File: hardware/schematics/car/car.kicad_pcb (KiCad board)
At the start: 2 copper layers, 30.2 x 17.9 mm, 18 parts, among them M1 Motor_Servo, Q1 Q_PMOS_Depletion, SW1 RotaryEncoder, SW2 SW_Push, SW3 SW_Push, U1 VL53L0CXV0DH1, U10 Mini-560, U2 VL53L0CXV0DH1, U3 VL53L0CXV0DH1, U4 Pixy2, U5 TXS0108EPW, U6 TB6612FNG, U7 SparkFun OTOS, U9 Mini-360

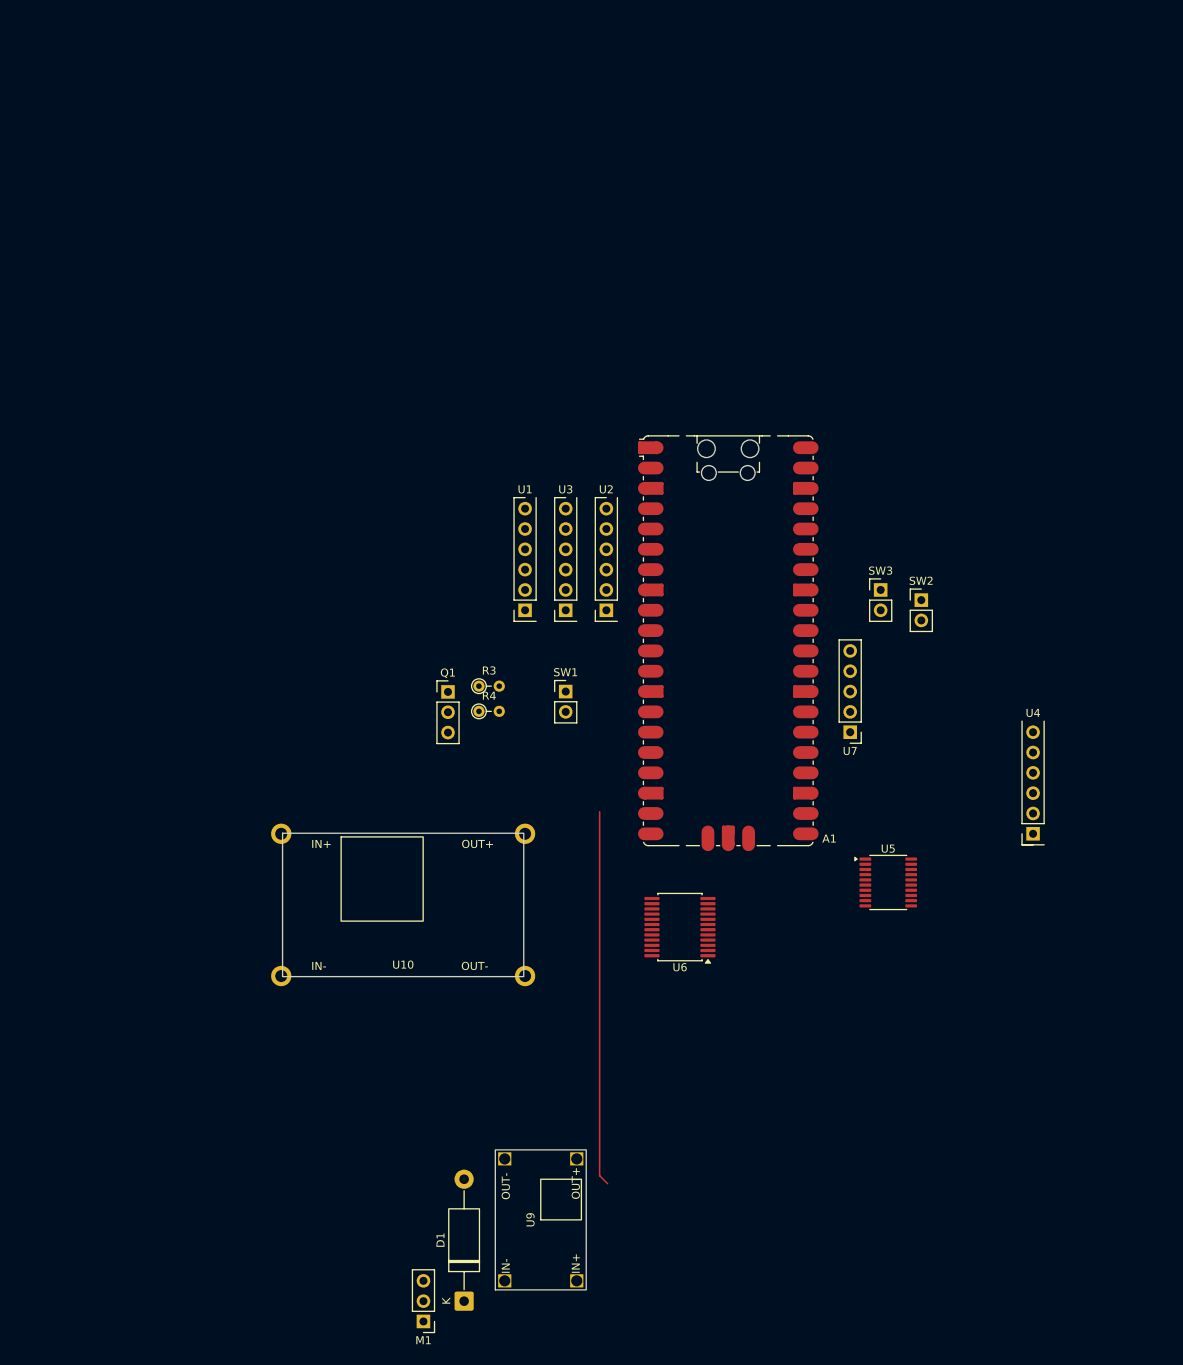
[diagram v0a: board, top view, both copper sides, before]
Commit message: [Schematic] update pcb components
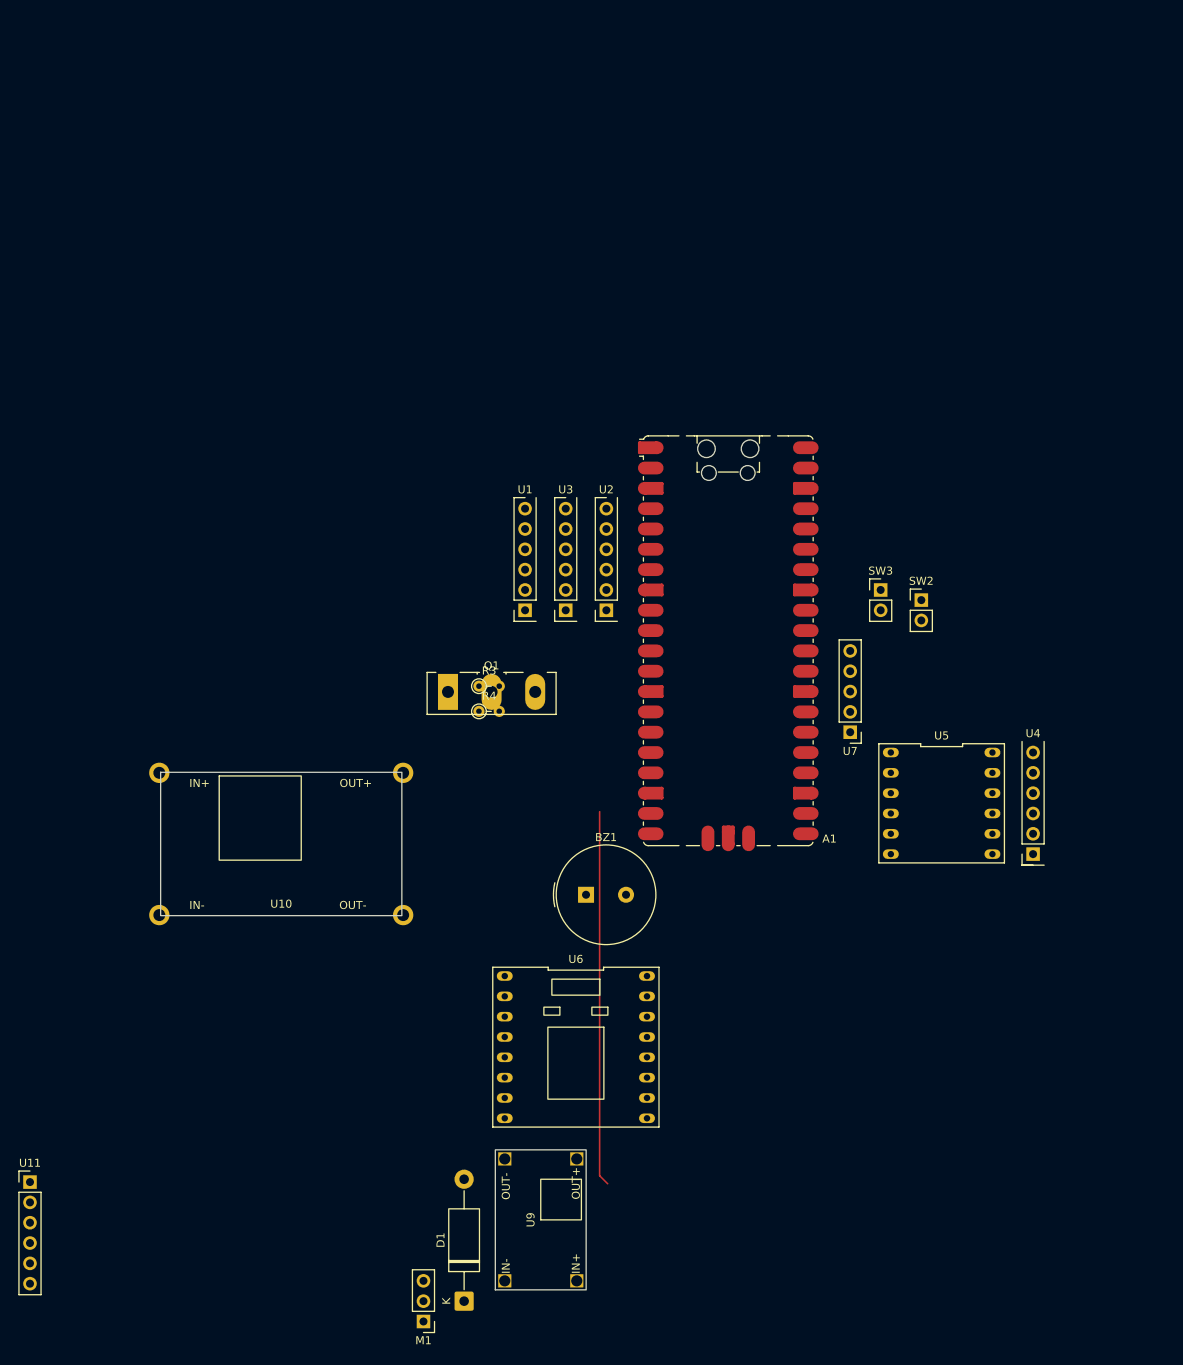
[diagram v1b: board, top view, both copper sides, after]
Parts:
- removed SW1: RotaryEncoder, Connector_PinHeader_2.54mm:PinHeader_1x02_P2.54mm_Vertical
- added BZ1: Buzzer, Buzzer_Beeper:Buzzer_TDK_PS1240P02BT_D12.2mm_H6.5mm, F.Cu at (114.3, 119.4)
- added U11: JGA25-37x, Connector_PinHeader_2.54mm:PinHeader_1x06_P2.54mm_Vertical, F.Cu at (44.8, 155.3)
- Q1: value Q_PMOS_Depletion -> PMOS; footprint Connector_PinHeader_2.54mm:PinHeader_1x03_P2.54mm_Vertical -> Package_TO_SOT_THT:TO-247-3_Vertical
- U5: value TXS0108EPW -> Level shifter; footprint Package_SO:TSSOP-20_4.4x6.5mm_P0.65mm -> xlnc-foot:LevelShifter_4channel_bidirectional
- U6: footprint Package_SO:SSOP-24_5.3x8.2mm_P0.65mm -> xlnc-foot:TB6612FNG_Breakout_Sparkfun
- moved U6 19.9 mm to (113.0, 138.4), turned to -90 degrees
- moved U10 17.0 mm to (76.2, 113.0)
- moved U5 11.9 mm to (158.8, 108.0), turned to -90 degrees
- moved U4 2.54 mm to (170.2, 101.6)
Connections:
- Q1 pad 1: (no net) -> +5V
- Q1 pad 2: (no net) -> Net-(A1-VBUS)
- Q1 pad 3: (no net) -> Net-(A1-VSYS)
- U5 pad 1: Net-(A1-GPIO16) -> Net-(A1-GPIO19)
- U5 pad 10: +3.3V -> +5V
- U5 pad 11: GND -> Net-(U4-SPI_SCK)
- U5 pad 12: unconnected-(U5-B8-Pad12) -> Net-(U4-MOSI/TX)
- U5 pad 2: +3.3V -> Net-(A1-GPIO18)
- U5 pad 3: Net-(A1-GPIO17) -> +3.3V
- U5 pad 4: Net-(A1-GPIO18) -> GND
- U5 pad 5: Net-(A1-GPIO19) -> Net-(A1-GPIO17)
- U5 pad 6: unconnected-(U5-A5-Pad6) -> Net-(A1-GPIO16)
- U5 pad 7: unconnected-(U5-A6-Pad7) -> Net-(U4-MISO/RX)
- U5 pad 8: unconnected-(U5-A7-Pad8) -> Net-(U4-SPI_SS)
- U5 pad 9: unconnected-(U5-A8-Pad9) -> GND
- U6 pad 1: Net-(M2-+) -> Net-(U11-M1)
- U6 pad 5: Net-(M2--) -> Net-(U11-M2)

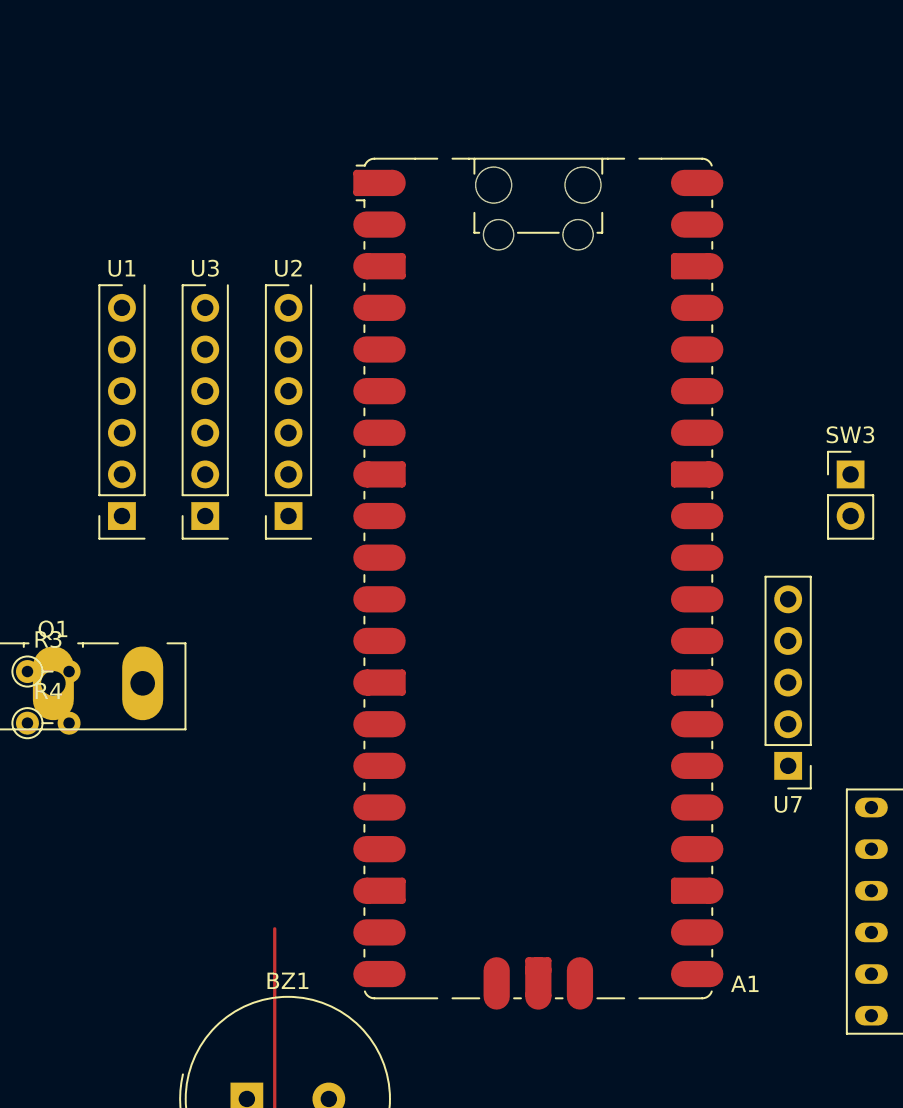
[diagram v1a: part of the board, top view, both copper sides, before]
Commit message: [Schematic] Some pcb movings
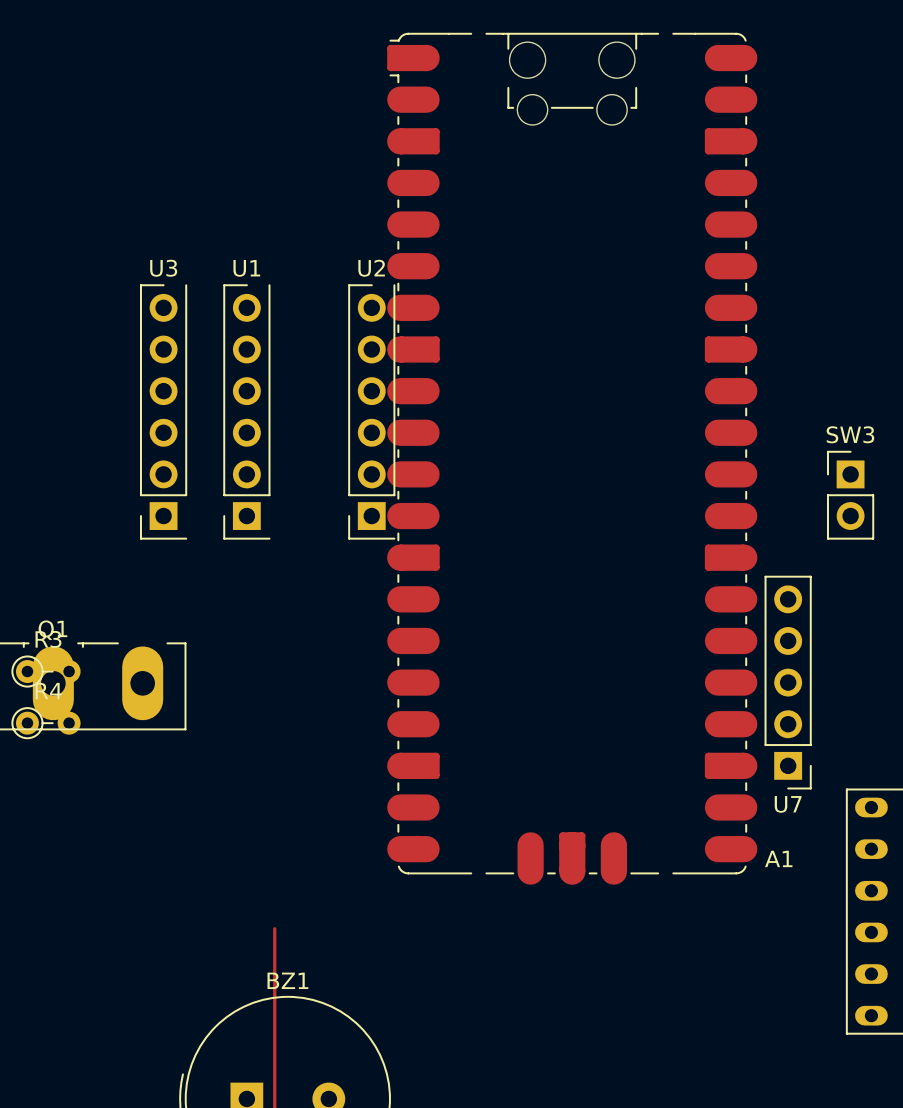
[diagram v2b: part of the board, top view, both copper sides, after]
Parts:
- moved A1 7.90 mm to (134.2, 80.0)
- moved U1 7.62 mm to (114.3, 71.1)
- moved U2 5.08 mm to (121.9, 71.1)
- moved U3 2.54 mm to (109.2, 71.1)

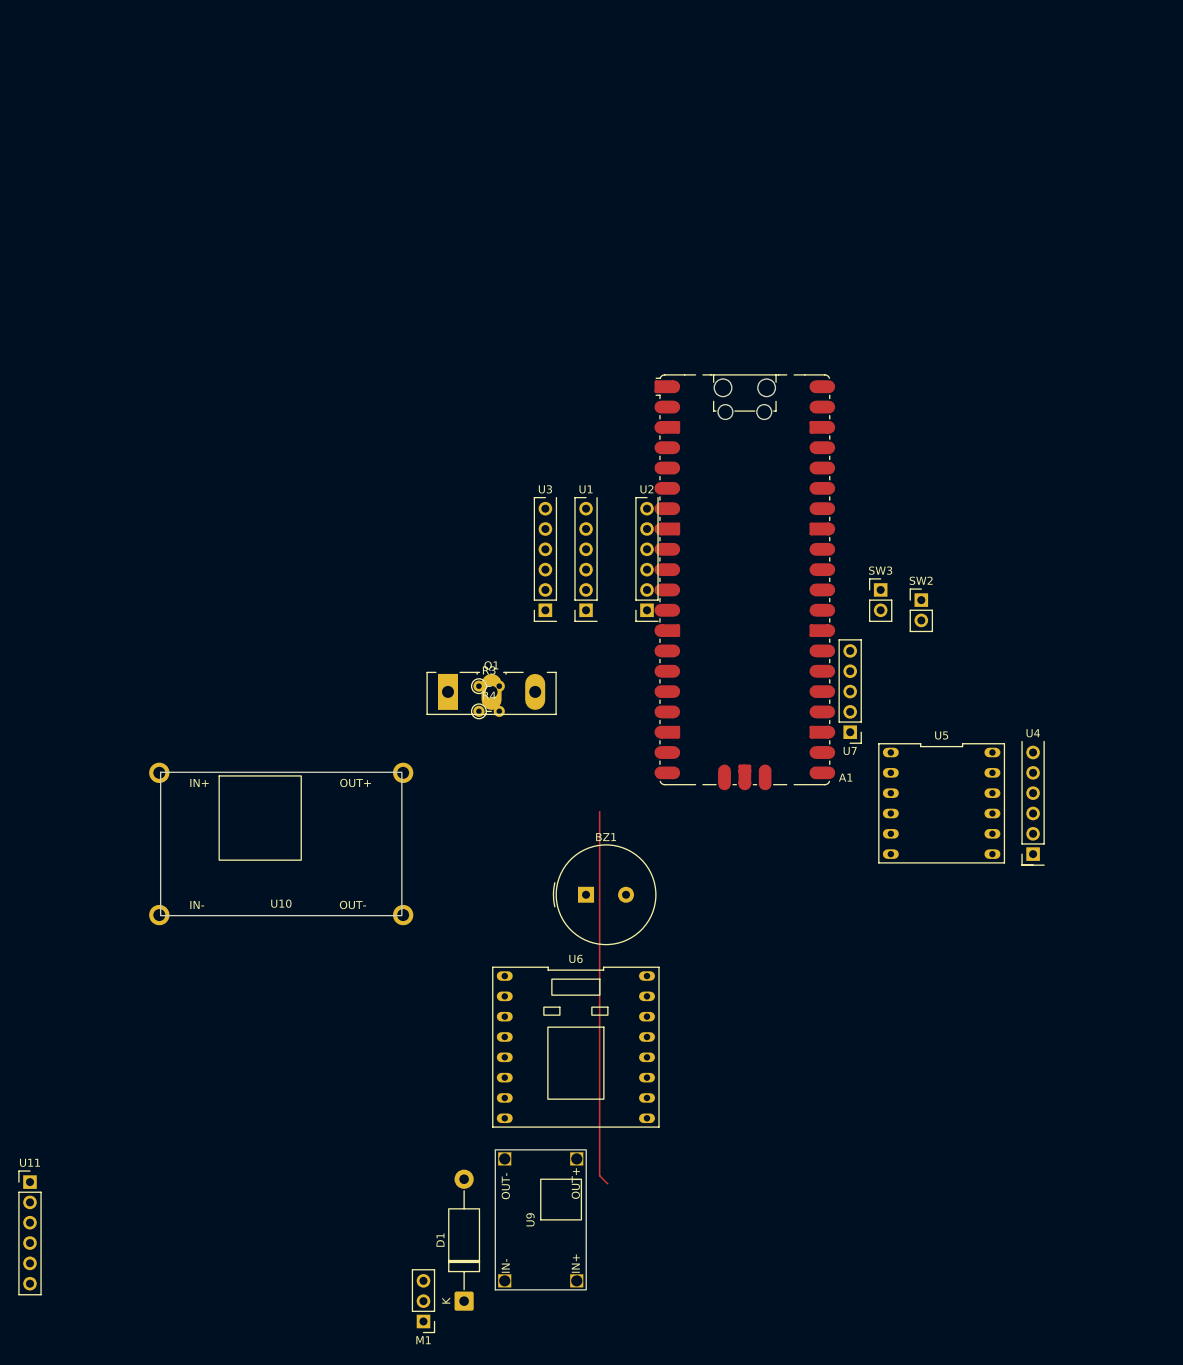
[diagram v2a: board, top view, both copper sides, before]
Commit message: [Schematic] Change button footprint. PCB: move around, connect easy things.
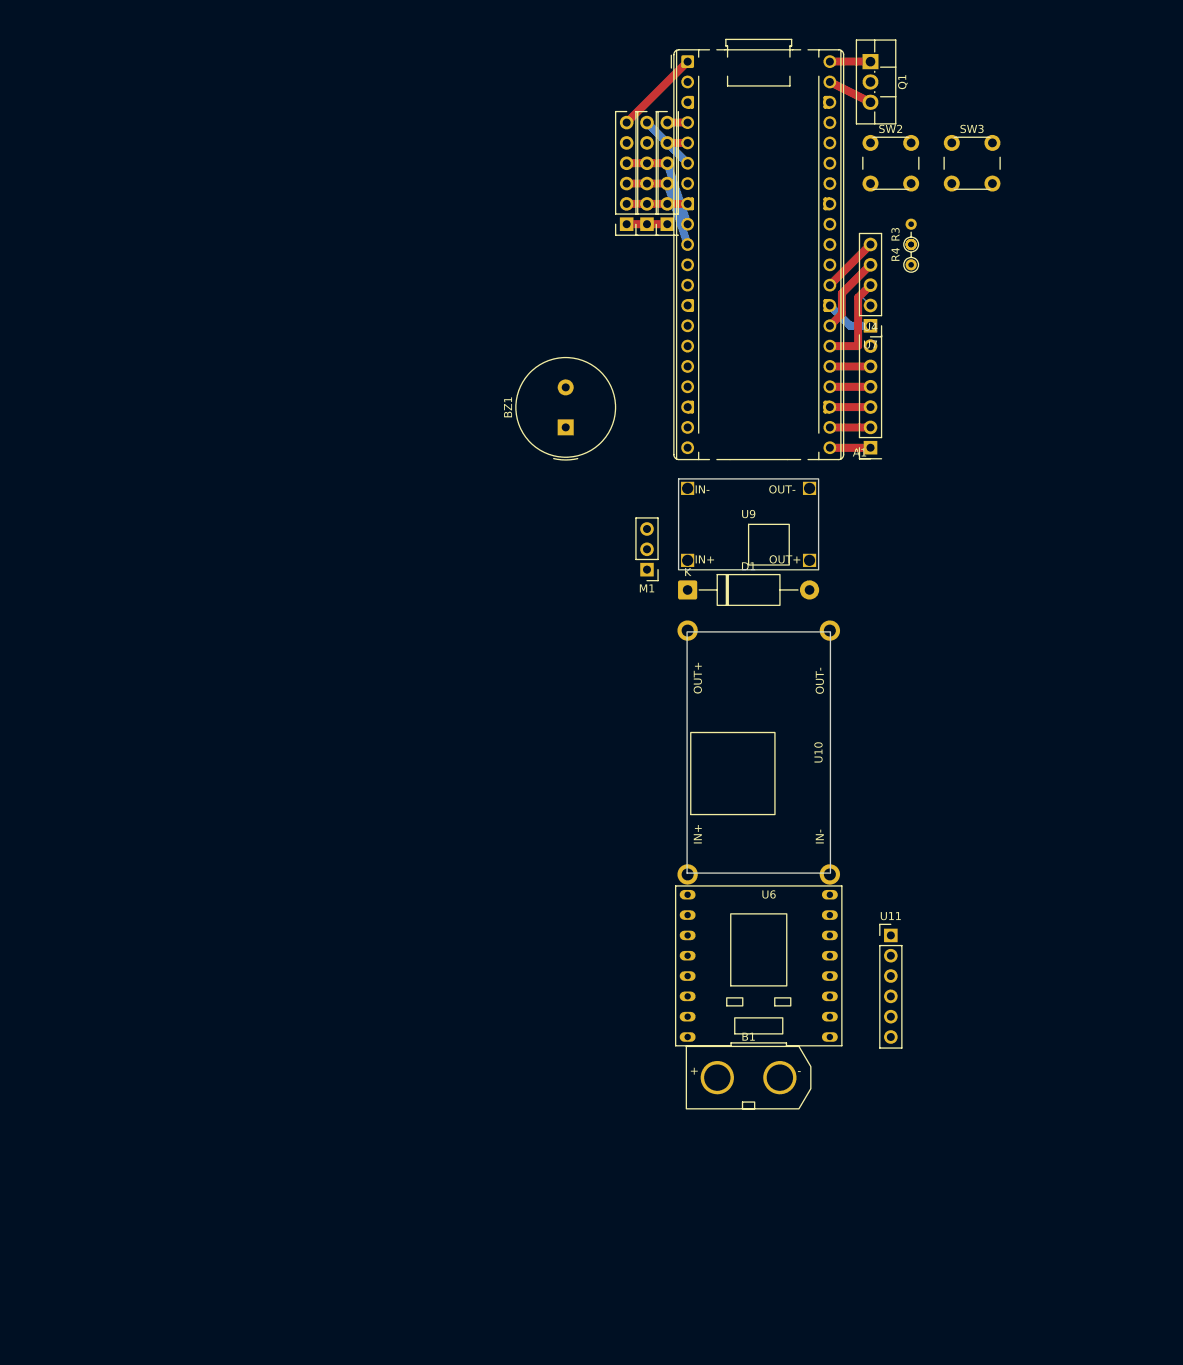
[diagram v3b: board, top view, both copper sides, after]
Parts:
- removed U5: Level shifter, xlnc-foot:LevelShifter_4channel_bidirectional
- added B1: XT60, xlnc-foot:XT60, F.Cu at (134.6, 142.2)
- A1: footprint Module:RaspberryPi_Pico_SMD_HandSolder -> Module:RaspberryPi_Pico_Common_THT
- Q1: footprint Package_TO_SOT_THT:TO-247-3_Vertical -> Package_TO_SOT_THT:TO-220F-3_Vertical
- SW2, SW3: footprint Connector_PinHeader_2.54mm:PinHeader_1x02_P2.54mm_Vertical -> xlnc-foot:SW_PUSH_6mm_5.08mm
- moved U11 111.9 mm to (152.4, 124.5)
- moved M1 98.0 mm to (121.9, 78.7)
- moved Q1 94.8 mm to (149.9, 15.2), turned to -90 degrees
- moved D1 93.2 mm to (127.0, 81.3), turned to 0 degrees
- moved U9 90.7 mm to (134.6, 73.1), turned to 0 degrees
- moved R4 77.7 mm to (154.9, 40.6), turned to 90 degrees
- moved R3 77.2 mm to (154.9, 38.1), turned to 90 degrees
- moved A1 65.2 mm to (127.0, 15.2)
- moved U10 60.8 mm to (135.9, 101.6), turned to 90 degrees
- moved BZ1 58.5 mm to (111.8, 61.0), turned to 90 degrees
- moved SW2 54.7 mm to (152.4, 27.9)
- moved U4 54.7 mm to (149.9, 50.8)
- moved SW3 54.6 mm to (162.6, 27.9)
- moved U7 50.9 mm to (149.9, 48.3)
- moved U3 49.3 mm to (119.4, 22.9)
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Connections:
- Q1 pad 1: +5V -> Net-(A1-VBUS)
- Q1 pad 2: Net-(A1-VBUS) -> +5V
- U4 pad 1: Net-(U4-MISO/RX) -> Net-(A1-GPIO16)
- U4 pad 3: Net-(U4-SPI_SCK) -> Net-(A1-GPIO18)
- U4 pad 4: Net-(U4-MOSI/TX) -> Net-(A1-GPIO19)
- U4 pad 7: Net-(U4-SPI_SS) -> Net-(A1-GPIO17)
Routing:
- net +3.3V: track 0.00 -> 60.0 mm
- net Net-(D1-K): track 46.9 -> 0.00 mm
- net GND: track 0.00 -> 18.8 mm
- net Net-(A1-GPIO7): track 0.00 -> 13.1 mm, vias 0 -> 1
- net Net-(A1-GPIO6): track 0.00 -> 13.1 mm
- net Net-(A1-GPIO20): track 0.00 -> 11.8 mm
- net Net-(A1-GPIO1): track 0.00 -> 10.8 mm
- net Net-(A1-GPIO0): track 0.00 -> 10.8 mm
- net Net-(A1-GPIO21): track 0.00 -> 9.72 mm
- net Net-(A1-GPIO22): track 0.00 -> 7.18 mm
- net Net-(A1-GPIO5): track 0.00 -> 7.18 mm
- net Net-(A1-GPIO4): track 0.00 -> 7.18 mm
- net Net-(A1-VSYS): track 0.00 -> 5.68 mm
- net Net-(A1-VBUS): track 0.00 -> 5.08 mm
- net Net-(A1-GPIO19): track 0.00 -> 5.08 mm
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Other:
- board size 30.2 x 17.9 mm -> 17.9 x 30.1 mm
- copper layers 2 -> 12
